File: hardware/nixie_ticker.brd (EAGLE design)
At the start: 127 x 61 mm, 12 parts

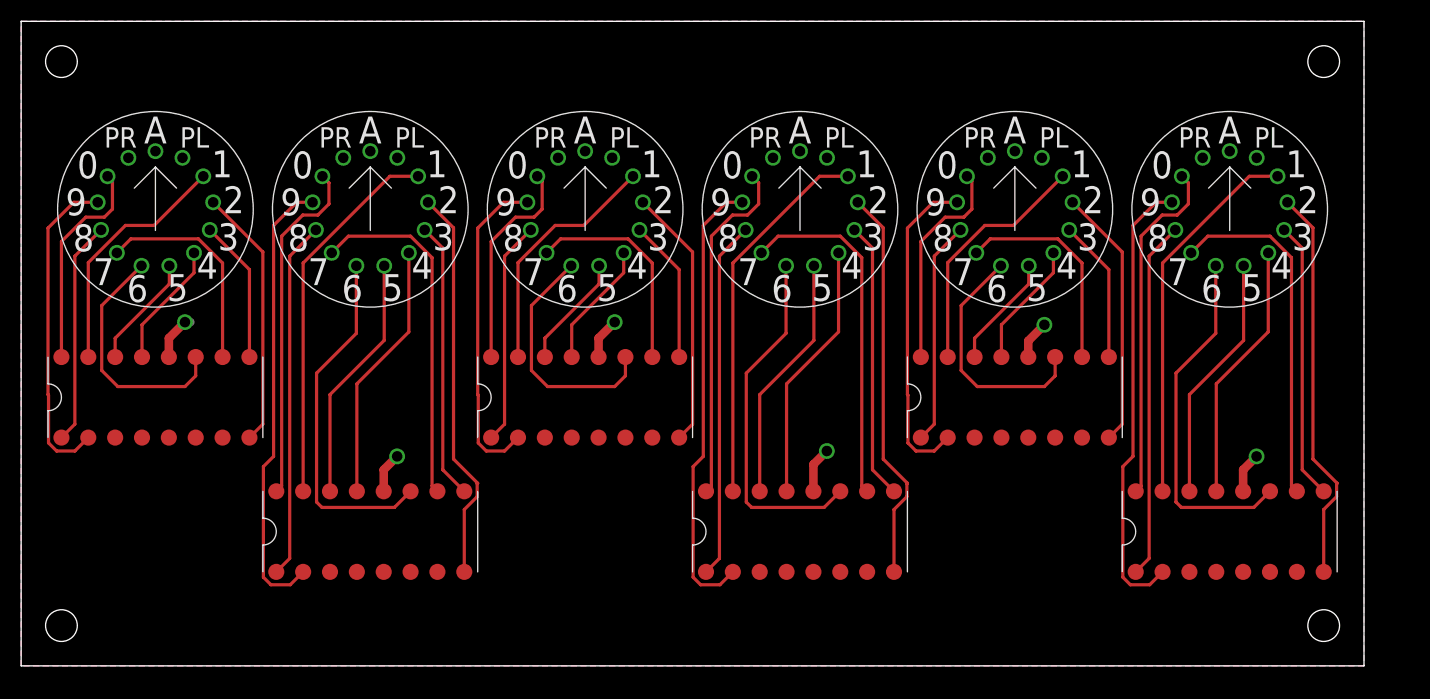
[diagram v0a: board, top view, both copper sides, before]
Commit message: Adding high voltage logo
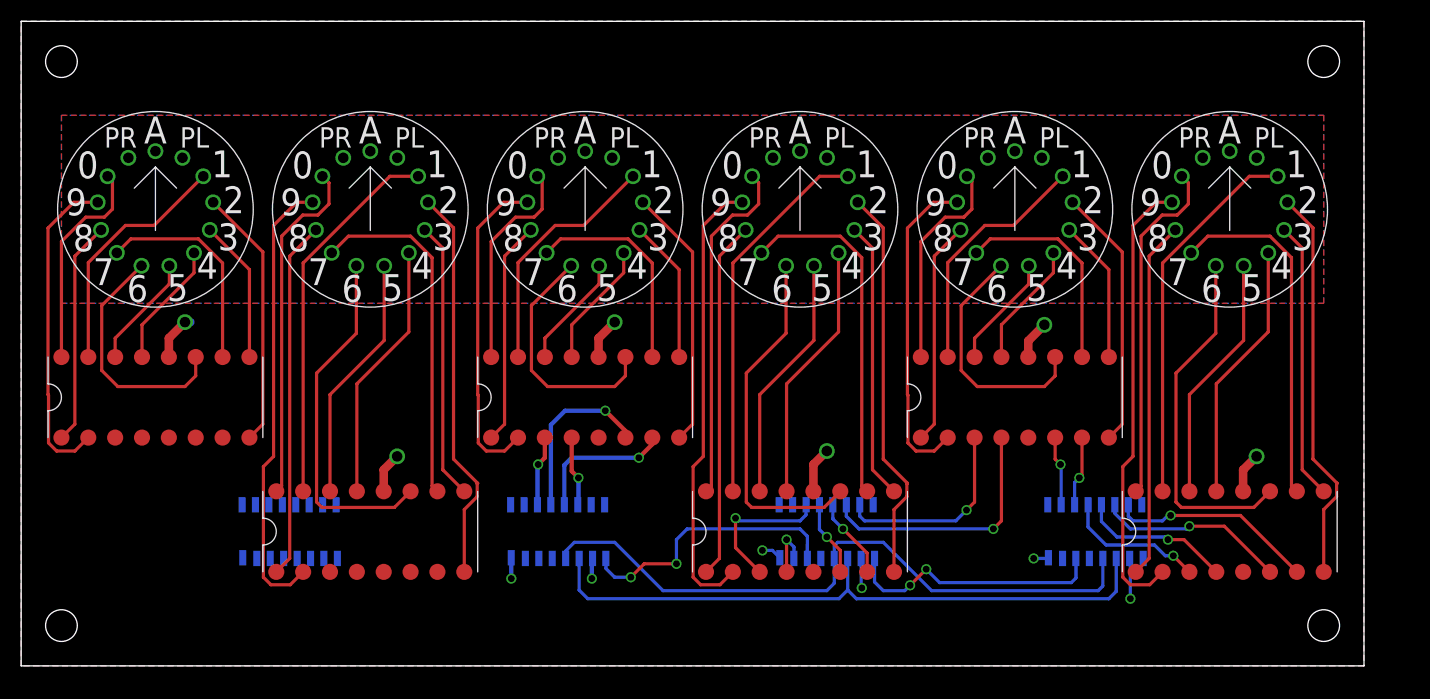
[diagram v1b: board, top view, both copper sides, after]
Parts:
- added U$10, U$3, U$4, U$9: 74AHC595, nixie_ticker:16SOIC
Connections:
- new net N$101: U$10.P$2, U$16.P$6
- new net N$21: U$4.P$9, U$9.P$14
- new net N$22: U$3.P$9, U$4.P$14
- new net N$23: U$10.P$14, U$9.P$9
- new net N$24: U$3.P$15, U$7.P$3
- new net N$25: U$3.P$1, U$7.P$6
- new net N$26: U$3.P$2, U$7.P$7
- new net N$27: U$3.P$3, U$7.P$4
- new net N$28: U$3.P$4
- new net N$29: U$3.P$5, U$8.P$3
- new net N$30: U$3.P$6, U$8.P$6
- new net N$41: U$3.P$7, U$8.P$7
- new net N$42: U$4.P$1
- new net N$43: U$4.P$2
- new net N$44: U$4.P$3, U$6.P$3
- new net N$45: U$4.P$4, U$6.P$6
- new net N$46: U$4.P$5, U$6.P$7
- new net N$47: U$4.P$15, U$8.P$4
- new net N$48: U$4.P$6, U$6.P$4
- new net N$49: U$4.P$7
- new net N$50: U$12.P$3, U$9.P$3
- new net N$51: U$12.P$6, U$9.P$4
- new net N$52: U$12.P$7, U$9.P$5
- new net N$53: U$12.P$4, U$9.P$15
- new net N$54: U$16.P$3, U$9.P$7
- new net N$55: U$9.P$1
- new net N$56: U$9.P$2
- new net N$58: U$10.P$3, U$16.P$7
- new net N$59: U$16.P$4, U$9.P$6
- new net N$60: U$10.P$1
- new net N$81: U$10.P$4, U$20.P$3
- new net N$82: U$10.P$6, U$20.P$6
- new net N$83: U$10.P$7, U$20.P$7
- new net N$84: U$10.P$5, U$20.P$4
- new net N$85: U$10.P$15
- new net N$86: U$10.P$12, U$3.P$12, U$4.P$12, U$9.P$12
- new net N$87: U$10.P$11, U$3.P$11, U$4.P$11, U$9.P$11
- new net N$88: U$3.P$14
- net +5V: now also U$10.P$10, U$10.P$16, U$3.P$10, U$3.P$16, U$4.P$10, U$4.P$16, U$9.P$10, U$9.P$16
- net GND: now also U$10.P$13, U$10.P$8, U$3.P$13, U$3.P$8, U$4.P$13, U$4.P$8, U$9.P$13, U$9.P$8
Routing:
- net N$86: track 0.00 -> 63.0 mm
- net N$87: track 0.00 -> 61.2 mm
- net N$21: track 0.00 -> 27.3 mm, vias 0 -> 2
- net N$23: track 0.00 -> 25.0 mm, vias 0 -> 2
- net N$59: track 0.00 -> 24.4 mm, vias 0 -> 1
- net N$83: track 0.00 -> 19.6 mm, vias 0 -> 1
- net N$54: track 0.00 -> 19.0 mm, vias 0 -> 1
- net N$82: track 0.00 -> 18.0 mm, vias 0 -> 1
- net N$45: track 0.00 -> 16.6 mm, vias 0 -> 1
- net N$84: track 0.00 -> 14.4 mm, vias 0 -> 1
- net N$50: track 0.00 -> 14.0 mm, vias 0 -> 1
- net +5V: track 0.00 -> 13.9 mm, vias 0 -> 6
- net N$46: track 0.00 -> 13.5 mm, vias 0 -> 1
- net N$81: track 0.00 -> 13.4 mm, vias 0 -> 1
- net N$52: track 0.00 -> 7.69 mm, vias 0 -> 1
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- added copper zone on layer 16, net N$89
- added copper zone on layer 1, net N$90
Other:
- board text added: "C:/Users/bmbou/Desktop/Stop_high_voltage_ukrainian_sign.bmp"

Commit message: Adding optocouplers to drive anodes
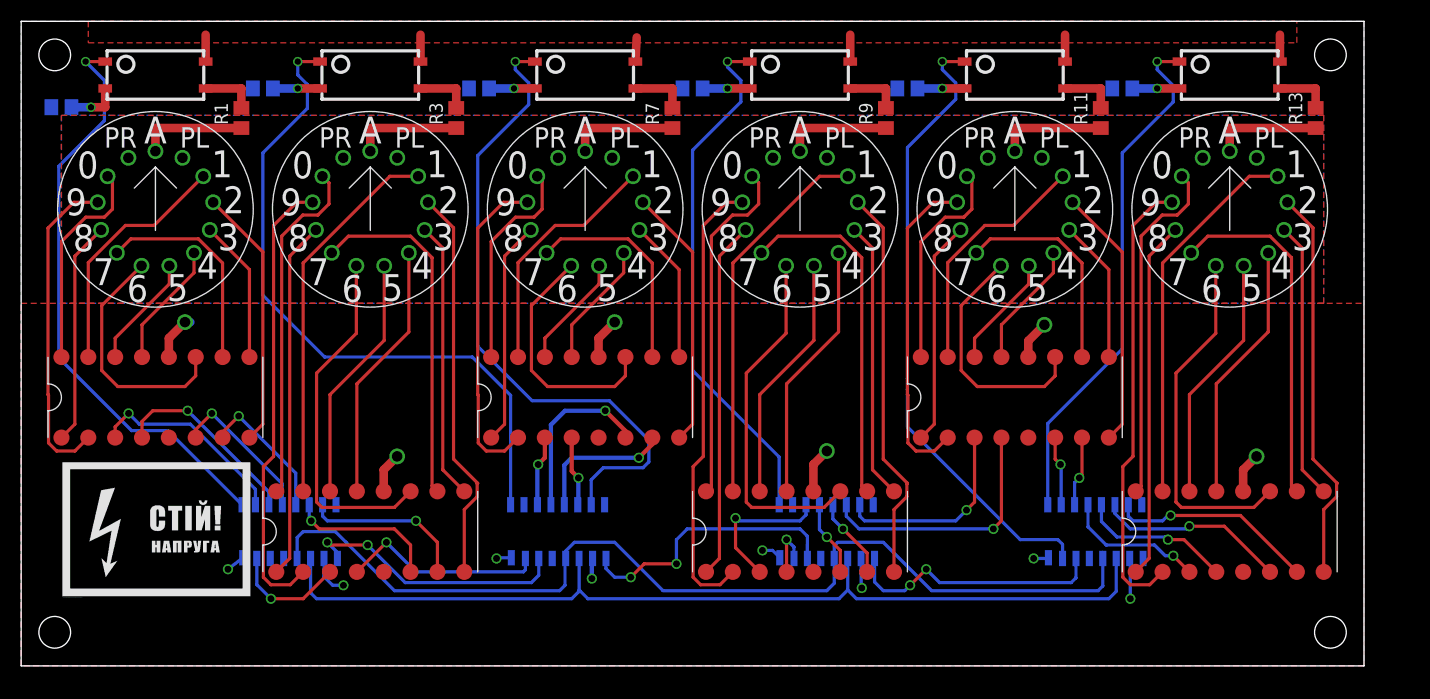
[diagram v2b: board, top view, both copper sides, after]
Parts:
- added R1, R10, R11, R12, R13, R14, R2, R3, R4, R7, R8, R9: (no value), resistor:R0805
- added U$13, U$14, U$18, U$21, U$22, U$23: TLP387, nixie_ticker:6-SOIC(4PIN)
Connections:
- removed net N$42 (its old number): U$4.P$1
- removed net N$55 (its old number): U$9.P$1
- new net N$102: R1.2, U$13.P$4
- new net N$103: R2.2, U$13.P$3
- new net N$104: R13.1, U$19.P$1
- new net N$105: R3.1, U$2.P$1
- new net N$106: R3.2, U$14.P$4
- new net N$107: R4.2, U$14.P$3
- new net N$112: R7.2, U$18.P$4
- new net N$113: R8.2, U$18.P$3
- new net N$118: R7.1, U$5.P$1
- new net N$119: R9.2, U$21.P$4
- new net N$120: R10.2, U$21.P$3
- new net N$145: R9.1, U$11.P$1
- new net N$146: R11.2, U$22.P$4
- new net N$147: R12.2, U$22.P$3
- new net N$153: R13.2, U$23.P$4
- new net N$154: R14.2, U$23.P$3
- new net N$43: U$14.P$1, U$4.P$1
- new net N$56: U$21.P$1, U$9.P$1
- new net N$57: R1.1, U$1.P$1
- new net N$90: R11.1, U$15.P$1
- new net V+: U$13.P$6, U$14.P$6, U$18.P$6, U$21.P$6, U$22.P$6, U$23.P$6
- net GND: now also R10.1, R12.1, R14.1, R2.1, R4.1, R8.1
- net N$24: now also U$3.P$2; no longer U$3.P$15
- net N$25: now also U$3.P$4; no longer U$3.P$1
- net N$26: now also U$3.P$5; no longer U$3.P$2
- net N$28: now also U$13.P$1, U$3.P$1; no longer U$3.P$4
- net N$29: now also U$3.P$15; no longer U$3.P$5
- net N$49: now also U$18.P$1
- net N$60: now also U$10.P$15, U$22.P$1; no longer U$10.P$1
- net N$85: now also U$10.P$1, U$23.P$1; no longer U$10.P$15
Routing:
- net N$43: track 0.00 -> 64.0 mm, vias 0 -> 1
- net N$49: track 0.00 -> 61.7 mm, vias 0 -> 1
- net N$60: track 0.00 -> 59.7 mm, vias 0 -> 1
- net N$28: track 0.00 -> 55.5 mm, vias 0 -> 1
- net N$56: track 0.00 -> 49.8 mm, vias 0 -> 1
- net N$85: track 0.00 -> 49.6 mm, vias 0 -> 1
- net N$86: track 63.0 -> 95.6 mm
- net N$87: track 61.2 -> 90.4 mm
- net N$22: track 0.00 -> 25.4 mm, vias 0 -> 2
- net N$47: track 0.00 -> 19.4 mm, vias 0 -> 1
- net N$24: track 0.00 -> 19.2 mm, vias 0 -> 1
- net N$27: track 0.00 -> 18.3 mm, vias 0 -> 1
- net N$41: track 0.00 -> 15.8 mm, vias 0 -> 1
- net V+: track 0.00 -> 15.1 mm
- net N$30: track 0.00 -> 14.5 mm, vias 0 -> 1
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- added copper zone on layer 1, net V+
- removed copper zone on layer 1, net N$90

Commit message: Adding high-voltage rail
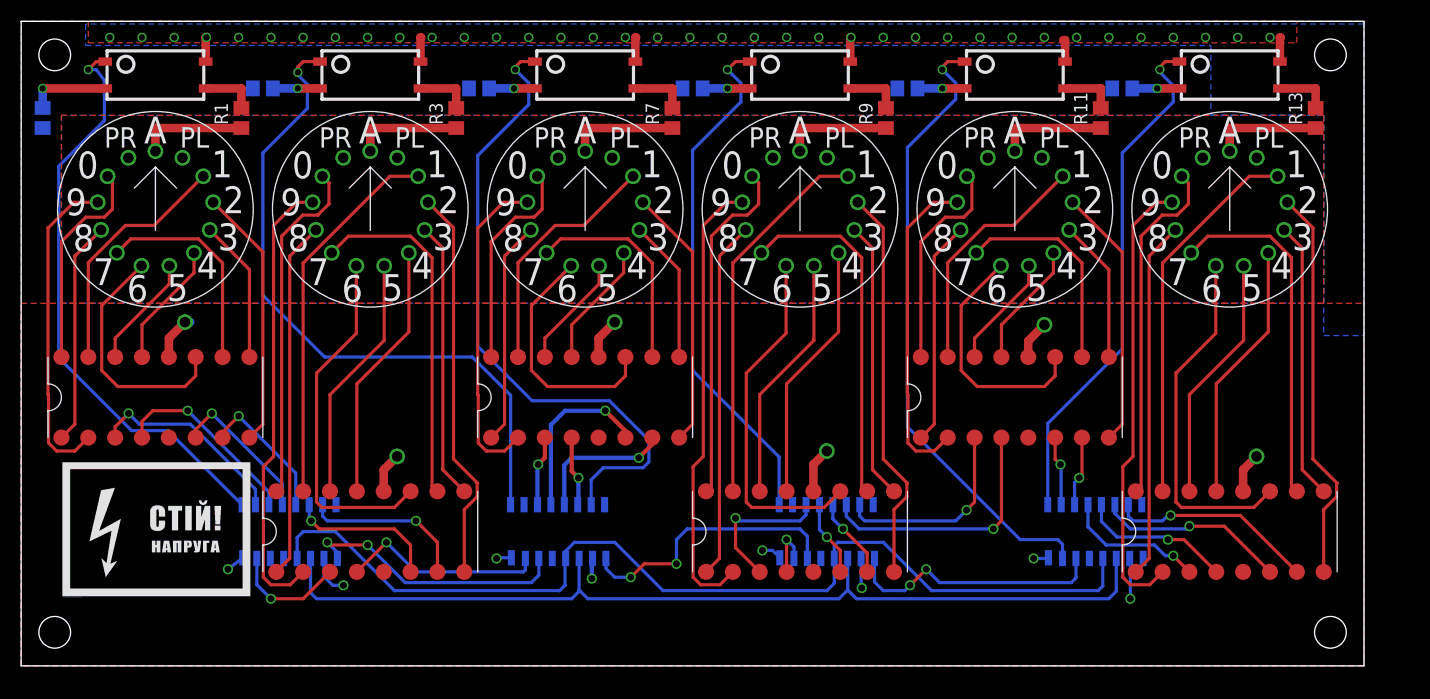
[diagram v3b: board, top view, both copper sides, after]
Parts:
- moved R2 2.05 mm to (2.03, 51.8), turned to 90 degrees
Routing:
- net N$103: track 4.97 -> 7.76 mm
- net V+: track 15.1 -> 14.1 mm, vias 0 -> 37
- added copper zone on layer 16, net V+

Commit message: Updates 6-29
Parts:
- moved R2 9.76 mm to (11.4, 54.6), turned to 0 degrees
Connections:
- net N$42: now also U$4.P$5; no longer U$4.P$2
- net N$43: now also U$4.P$2; no longer U$4.P$1
- net N$45: now also U$4.P$6; no longer U$4.P$4
- net N$46: now also U$4.P$7; no longer U$4.P$5
- net N$48: now also U$4.P$4; no longer U$4.P$6
- net N$49: now also U$4.P$1; no longer U$4.P$7
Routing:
- net N$86: track 95.6 -> 126.6 mm, vias 0 -> 2
- net N$49: track 61.4 -> 47.4 mm
- net N$56: track 49.4 -> 60.1 mm, vias 1 -> 3
- net N$45: track 16.6 -> 8.85 mm
- net +5V: track 19.0 -> 25.2 mm
- net N$46: track 13.5 -> 9.53 mm
- net N$21: track 27.3 -> 23.8 mm, vias 2 -> 0
- net N$97: track 23.2 -> 21.1 mm
- net N$103: track 7.76 -> 5.69 mm
- net N$60: track 59.4 -> 61.3 mm
- net N$53: track 5.12 -> 6.62 mm
- net N$85: track 49.3 -> 48.0 mm
- net N$87: track 90.4 -> 91.7 mm
- net N$28: track 55.1 -> 53.9 mm
- net N$48: track 6.64 -> 7.17 mm
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- added copper zone on layer 1, net GND
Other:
- board text added: "https://github.com/bmboucher/nixie_ticker"

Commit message: Updates 6-29
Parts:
- added C1, C10, C11, C12, C13, C14, C2, C3, C4, C5, C6, C7, C8, C9: (no value), resistor:C0402
- added R15, R16, R5, R6: (no value), resistor:R0402
- added SV1: (no value), con-lstb:MA03-2
- added U$17, U$24: ZKFDS, nixie_ticker:ZKFDS
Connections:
- new net N$108: C2.1, R6.1, U$4.P$10
- new net N$109: C1.1, R5.1, U$3.P$10
- new net N$110: C3.1, R15.1, U$9.P$10
- new net N$111: C8.1, R16.1, U$10.P$10
- new net N$159: SV1.4
- net +5V: now also C10.1, C11.1, C12.1, C13.1, C14.1, C4.1, C5.1, C6.1, C7.1, C9.1, R15.2, R16.2, R5.2, R6.2, SV1.6; no longer U$10.P$10, U$3.P$10, U$4.P$10, U$9.P$10
- net GND: now also C1.2, C10.2, C11.2, C12.2, C13.2, C14.2, C2.2, C3.2, C4.2, C5.2, C6.2, C7.2, C8.2, C9.2, SV1.2, U$24.P$1, U$24.P$2
- net N$86: now also SV1.1
- net N$87: now also SV1.3
- net N$88: now also SV1.5
- net V+: now also U$17.P$1, U$17.P$2
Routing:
- net N$86: track 126.6 -> 108.2 mm, vias 2 -> 3
- net N$110: track 0.00 -> 18.0 mm, vias 0 -> 1
- net GND: track 24.0 -> 37.3 mm, vias 55 -> 63
- net N$108: track 0.00 -> 10.8 mm, vias 0 -> 1
- net N$109: track 0.00 -> 8.22 mm
- net N$111: track 0.00 -> 7.61 mm
- net +5V: track 25.2 -> 19.8 mm, vias 8 -> 6
- net N$60: track 61.3 -> 66.3 mm
- net N$22: track 25.4 -> 22.9 mm, vias 2 -> 0
- net N$7: track 23.2 -> 22.2 mm
- net N$87: track 91.7 -> 90.7 mm
- net N$1: track 20.3 -> 21.3 mm
- net N$40: track 30.7 -> 31.5 mm
- net N$11: track 32.9 -> 33.7 mm
- net N$10: track 30.7 -> 31.4 mm
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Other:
- board text removed: "C:/Users/bmbou/Desktop/Stop_high_voltage_ukrainian_sign.bmp"

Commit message: Finalizing board 7-1
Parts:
- removed SV1: (no value), con-lstb:MA03-2
- added C15, C16: (no value), resistor:C0402
- added JP1: (no value), pinhead:1X06
- added Q1, Q2: BCX19SMD, transistor-npn:SOT23-BEC
- added R17, R18: (no value), resistor:R0805
- added U$25: CD40109B, nixie_ticker:SOP65P640X120-16
- U$13, U$14, U$18, U$21, U$22, U$23: value TLP387 -> TLP3873D; device nixie_ticker:6-SOIC(4PIN) -> nixie_ticker:SOP254P1000X215-4
- moved C4 3.27 mm to (18.8, 9.78), turned to 0 degrees
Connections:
- new net +3V3: C16.1, JP1.3, U$25.1, U$25.15, U$25.2, U$25.7, U$25.9
- new net N$152: JP1.4, U$25.3
- new net N$160: Q1.C, R18.1
- new net N$161: Q2.C, R17.1
- new net N$162: R17.2, U$11.P$13
- new net N$163: R18.2, U$2.P$13
- net +5V: now also C15.1, JP1.2, U$25.16; no longer SV1.6
- net GND: now also C15.2, C16.2, JP1.1, Q1.E, Q2.E, U$25.8; no longer SV1.2
- net N$102: now also U$13.3; no longer U$13.P$4
- net N$103: now also U$13.2; no longer U$13.P$3
- net N$106: now also U$14.3; no longer U$14.P$4
- net N$107: now also U$14.2; no longer U$14.P$3
- net N$112: now also U$18.3; no longer U$18.P$4
- net N$113: now also U$18.2; no longer U$18.P$3
- net N$119: now also U$21.3; no longer U$21.P$4
- net N$120: now also U$21.2; no longer U$21.P$3
- net N$146: now also U$22.3; no longer U$22.P$4
- net N$147: now also U$22.2; no longer U$22.P$3
- net N$153: now also U$23.3; no longer U$23.P$4
- net N$154: now also U$23.2; no longer U$23.P$3
- net N$159: now also JP1.6, U$25.10; no longer SV1.4
- net N$22: now also U$25.11
- net N$28: now also U$13.1; no longer U$13.P$1
- net N$42: now also Q1.B, U$4.P$3; no longer U$4.P$5
- net N$43: now also U$14.1; no longer U$14.P$1
- net N$44: now also U$4.P$4; no longer U$4.P$3
- net N$48: now also U$4.P$5; no longer U$4.P$4
- net N$49: now also U$18.1; no longer U$18.P$1
- net N$55: now also Q2.B
- net N$56: now also U$21.1; no longer U$21.P$1
- net N$60: now also U$22.1; no longer U$22.P$1
- net N$85: now also U$23.1; no longer U$23.P$1
- net N$86: now also U$25.4; no longer SV1.1
- net N$87: now also U$25.5; no longer SV1.3
- net N$88: now also JP1.5, U$25.6; no longer SV1.5, U$3.P$14
- net V+: now also U$13.4, U$14.4, U$18.4, U$21.4, U$22.4, U$23.4; no longer U$13.P$6, U$14.P$6, U$18.P$6, U$21.P$6, U$22.P$6, U$23.P$6
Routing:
- net N$42: track 0.00 -> 55.9 mm
- net N$55: track 0.00 -> 55.1 mm, vias 0 -> 2
- net +3V3: track 0.00 -> 37.4 mm, vias 0 -> 3
- net N$22: track 22.9 -> 50.3 mm, vias 0 -> 2
- net N$87: track 90.7 -> 110.5 mm
- net N$159: track 0.00 -> 17.6 mm
- net N$86: track 108.2 -> 125.1 mm
- net N$160: track 0.00 -> 8.37 mm
- net N$161: track 0.00 -> 8.37 mm
- net N$44: track 6.69 -> 13.3 mm
- net N$152: track 0.00 -> 6.53 mm
- net N$88: track 0.00 -> 6.29 mm
- net N$163: track 0.00 -> 4.32 mm
- net N$162: track 0.00 -> 4.27 mm
- net N$43: track 63.5 -> 59.3 mm
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
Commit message: Updates 7-7
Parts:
- added CD40109B: CD40109B, nixie_ticker:SOP65P640X120-16
- added R19, R20, R21, R22, R23, R24: (no value), resistor:R0402
- U$25: value CD40109B -> UUR1C221MCL6GS; device nixie_ticker:SOP65P640X120-16 -> nixie_ticker:CAPAE830X1050
- moved U$25 17.6 mm to (17.0, 29.3), turned to 0 degrees
- moved C1 0.65 mm to (35.3, 10.8), turned to 90 degrees
- moved R5 0.63 mm to (33.9, 10.8), turned to 90 degrees
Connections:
- removed net N$152: JP1.4, U$25.3
- removed net N$159: JP1.6, U$25.10
- removed net N$86: U$10.P$12, U$25.4, U$3.P$12, U$4.P$12, U$9.P$12
- removed net N$87: U$10.P$11, U$25.5, U$3.P$11, U$4.P$11, U$9.P$11
- removed net N$88: JP1.5, U$25.6
- new net DI_L: CD40109B.10, JP1.6
- new net DS_1: CD40109B.11, R21.2, U$3.P$14
- new net SHCP_5V: CD40109B.5, R19.2, U$10.P$11, U$3.P$11, U$4.P$11, U$9.P$11
- new net SHCP_L: CD40109B.6, JP1.5
- new net STCP_5V: CD40109B.4, R20.2, U$10.P$12, U$3.P$12, U$4.P$12, U$9.P$12
- new net STCP_L: CD40109B.3, JP1.4
- net +3V3: now also CD40109B.1, CD40109B.15, CD40109B.2, CD40109B.7, CD40109B.9; no longer U$25.1, U$25.15, U$25.2, U$25.7, U$25.9
- net +5V: now also CD40109B.16, U$25.1; no longer U$25.16
- net GND: now also CD40109B.8, R19.1, R20.1, R21.1, R22.1, R23.1, R24.1, U$25.2; no longer U$25.8
- net N$21: now also R23.2
- net N$22: now also R22.2; no longer U$25.11
- net N$23: now also R24.2
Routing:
- net STCP_5V: track 0.00 -> 127.9 mm, vias 0 -> 3
- net N$86: track 125.1 -> 0.00 mm, vias 3 -> 0
- net SHCP_5V: track 0.00 -> 115.4 mm
- net N$87: track 110.5 -> 0.00 mm
- net DS_1: track 0.00 -> 28.7 mm, vias 0 -> 2
- net N$22: track 50.3 -> 23.0 mm, vias 2 -> 0
- net N$159: track 17.6 -> 0.00 mm
- net DI_L: track 0.00 -> 17.6 mm
- net STCP_L: track 0.00 -> 6.53 mm
- net N$152: track 6.53 -> 0.00 mm
- net SHCP_L: track 0.00 -> 6.29 mm
- net N$88: track 6.29 -> 0.00 mm
- net +5V: track 22.9 -> 25.9 mm, vias 7 -> 8
- net GND: track 37.3 -> 39.1 mm, vias 63 -> 67
- net N$23: track 25.0 -> 26.6 mm
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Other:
- board text added: "3V3"
- board text added: "5V"
- board text added: "DI"
- board text added: "GND"
- board text added: "SHCP"
- board text added: "STCP"
